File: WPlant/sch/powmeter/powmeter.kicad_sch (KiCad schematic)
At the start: 43 parts, among them J1 Input, J2 Out-L, J3 PROG/SWD, J4 Data, J5 Out-N, U1 BL0942, U2 PY32F003F18P6TU, U3 CA-IS3721CHS, U4 TLV70433DBVR

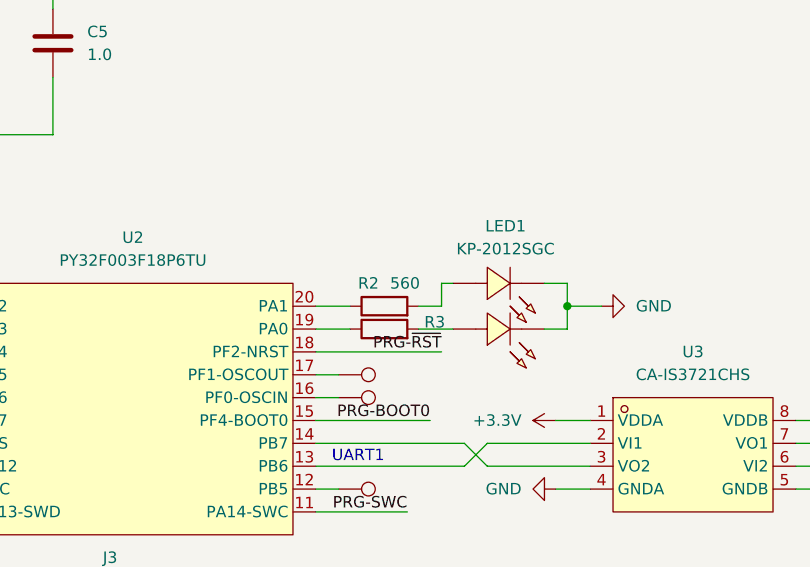
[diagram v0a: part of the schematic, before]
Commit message: Update WP Sch (sheets titles, replaced wires by bus, update components values)
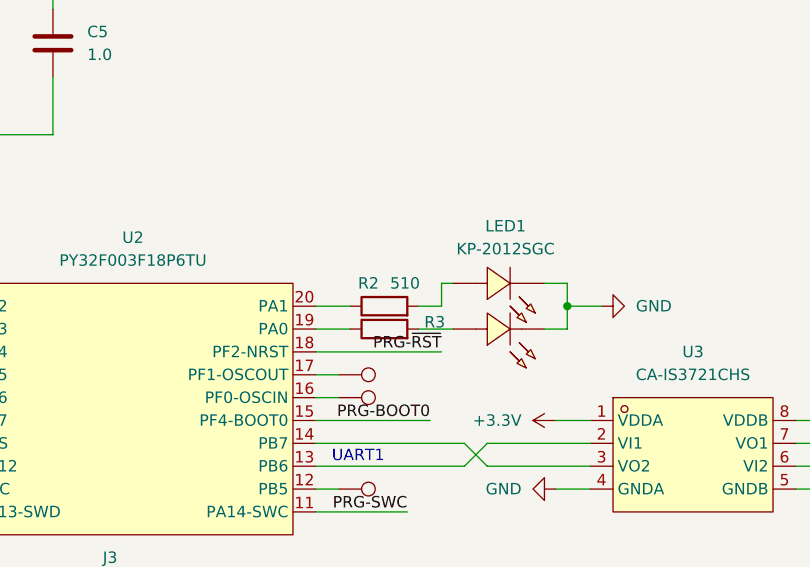
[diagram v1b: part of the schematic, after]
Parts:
- D4: value DSK34_C727076 -> DSK34
- R2, R3: value 560 -> 510
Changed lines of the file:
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@@
 			)
 		)
-		(property "Value" "DSK34_C727076"
+		(property "Value" "DSK34"
 			(at 44.45 128.27 0)
 			(effects
@@
 			)
 		)
-		(property "Value" "560"
+		(property "Value" "510"
 			(at 205.74 102.87 90)
 			(effects
@@
 			)
 		)
-		(property "Value" "560"
+		(property "Value" "510"
 			(at 208.026 101.6 90)
 			(effects
